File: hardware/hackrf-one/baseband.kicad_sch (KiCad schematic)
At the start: 98 parts, among them P14 XCVR_CLKOUT, P39 SSP1_SCK, P40 SSP1_COPI, P41 SSP1_CIPO, P53 CS_XCVR, P54 CS_AD, P56 RXENABLE, P61 DA0, P62 DA7, P63 DD0, P64 DD9, P65 DA4, P66 DD5, P67 RSSI, P83 GND, P84 GND, P85 GND, P86 GND, P87 GND, P88 GND, P89 GND, P9 BASEBAND, P90 GND, P91 GND, P92 GND, Q3 MOSFET_P, T3 RX_BALUN, T4 TX_BALUN, U17 MAX2839, U18 MAX5864

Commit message: HackRF One: update 100 nF capacitor part selection
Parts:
- C123, C167, C71, C73, C75, C77, C79, C81, C83, C91: Manufacturer Murata -> Samsung; Part Number GRM155R61A104KA01D -> CL05A104KA5NNNC
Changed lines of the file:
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@@
       (effects (font (size 1.524 1.524)) hide)
     )
-    (property "Manufacturer" "Murata" (id 4) (at 388.62 190.5 0)
-      (effects (font (size 1.524 1.524)) hide)
-    )
-    (property "Part Number" "GRM155R61A104KA01D" (id 5) (at 388.62 190.5 0)
-      (effects (font (size 1.524 1.524)) hide)
-    )
-    (property "Description" "CAP CER 0.1UF 10V 10% X5R 0402" (id 6) (at 388.62 190.5 0)
+    (property "Manufacturer" "Samsung" (id 4) (at 388.62 190.5 0)
+      (effects (font (size 1.524 1.524)) hide)
+    )
+    (property "Part Number" "CL05A104KA5NNNC" (id 5) (at 388.62 190.5 0)
+      (effects (font (size 1.524 1.524)) hide)
+    )
+    (property "Description" "CAP CER 0.1UF 25V X5R 0402" (id 6) (at 388.62 190.5 0)
       (effects (font (size 1.524 1.524)) hide)
     )
@@
       (effects (font (size 1.524 1.524)) hide)
     )
-    (property "Manufacturer" "Murata" (id 4) (at 303.53 30.48 0)
-      (effects (font (size 1.524 1.524)) hide)
-    )
-    (property "Part Number" "GRM155R61A104KA01D" (id 5) (at 303.53 30.48 0)
-      (effects (font (size 1.524 1.524)) hide)
-    )
-    (property "Description" "CAP CER 0.1UF 10V 10% X5R 0402" (id 6) (at 303.53 30.48 0)
+    (property "Manufacturer" "Samsung" (id 4) (at 303.53 30.48 0)
+      (effects (font (size 1.524 1.524)) hide)
+    )
+    (property "Part Number" "CL05A104KA5NNNC" (id 5) (at 303.53 30.48 0)
+      (effects (font (size 1.524 1.524)) hide)
+    )
+    (property "Description" "CAP CER 0.1UF 25V X5R 0402" (id 6) (at 303.53 30.48 0)
       (effects (font (size 1.524 1.524)) hide)
     )
@@
       (effects (font (size 1.524 1.524)) hide)
     )
-    (property "Manufacturer" "Murata" (id 4) (at 318.77 30.48 0)
-      (effects (font (size 1.524 1.524)) hide)
-    )
-    (property "Part Number" "GRM155R61A104KA01D" (id 5) (at 318.77 30.48 0)
-      (effects (font (size 1.524 1.524)) hide)
-    )
-    (property "Description" "CAP CER 0.1UF 10V 10% X5R 0402" (id 6) (at 318.77 30.48 0)
+    (property "Manufacturer" "Samsung" (id 4) (at 318.77 30.48 0)
+      (effects (font (size 1.524 1.524)) hide)
+    )
+    (property "Part Number" "CL05A104KA5NNNC" (id 5) (at 318.77 30.48 0)
+      (effects (font (size 1.524 1.524)) hide)
+    )
+    (property "Description" "CAP CER 0.1UF 25V X5R 0402" (id 6) (at 318.77 30.48 0)
       (effects (font (size 1.524 1.524)) hide)
     )
@@
       (effects (font (size 1.524 1.524)) hide)
     )
-    (property "Manufacturer" "Murata" (id 4) (at 334.01 30.48 0)
-      (effects (font (size 1.524 1.524)) hide)
-    )
-    (property "Part Number" "GRM155R61A104KA01D" (id 5) (at 334.01 30.48 0)
-      (effects (font (size 1.524 1.524)) hide)
-    )
-    (property "Description" "CAP CER 0.1UF 10V 10% X5R 0402" (id 6) (at 334.01 30.48 0)
+    (property "Manufacturer" "Samsung" (id 4) (at 334.01 30.48 0)
+      (effects (font (size 1.524 1.524)) hide)
+    )
+    (property "Part Number" "CL05A104KA5NNNC" (id 5) (at 334.01 30.48 0)
+      (effects (font (size 1.524 1.524)) hide)
+    )
+    (property "Description" "CAP CER 0.1UF 25V X5R 0402" (id 6) (at 334.01 30.48 0)
       (effects (font (size 1.524 1.524)) hide)
     )
@@
       (effects (font (size 1.524 1.524)) hide)
     )
-    (property "Manufacturer" "Murata" (id 4) (at 349.25 30.48 0)
-      (effects (font (size 1.524 1.524)) hide)
-    )
-    (property "Part Number" "GRM155R61A104KA01D" (id 5) (at 349.25 30.48 0)
-      (effects (font (size 1.524 1.524)) hide)
-    )
-    (property "Description" "CAP CER 0.1UF 10V 10% X5R 0402" (id 6) (at 349.25 30.48 0)
+    (property "Manufacturer" "Samsung" (id 4) (at 349.25 30.48 0)
+      (effects (font (size 1.524 1.524)) hide)
+    )
+    (property "Part Number" "CL05A104KA5NNNC" (id 5) (at 349.25 30.48 0)
+      (effects (font (size 1.524 1.524)) hide)
+    )
+    (property "Description" "CAP CER 0.1UF 25V X5R 0402" (id 6) (at 349.25 30.48 0)
       (effects (font (size 1.524 1.524)) hide)
     )
@@
       (effects (font (size 1.524 1.524)) hide)
     )
-    (property "Manufacturer" "Murata" (id 4) (at 364.49 30.48 0)
-      (effects (font (size 1.524 1.524)) hide)
-    )
-    (property "Part Number" "GRM155R61A104KA01D" (id 5) (at 364.49 30.48 0)
-      (effects (font (size 1.524 1.524)) hide)
-    )
-    (property "Description" "CAP CER 0.1UF 10V 10% X5R 0402" (id 6) (at 364.49 30.48 0)
+    (property "Manufacturer" "Samsung" (id 4) (at 364.49 30.48 0)
+      (effects (font (size 1.524 1.524)) hide)
+    )
+    (property "Part Number" "CL05A104KA5NNNC" (id 5) (at 364.49 30.48 0)
+      (effects (font (size 1.524 1.524)) hide)
+    )
+    (property "Description" "CAP CER 0.1UF 25V X5R 0402" (id 6) (at 364.49 30.48 0)
       (effects (font (size 1.524 1.524)) hide)
     )
@@
       (effects (font (size 1.524 1.524)) hide)
     )
-    (property "Manufacturer" "Murata" (id 4) (at 379.73 30.48 0)
-      (effects (font (size 1.524 1.524)) hide)
-    )
-    (property "Part Number" "GRM155R61A104KA01D" (id 5) (at 379.73 30.48 0)
-      (effects (font (size 1.524 1.524)) hide)
-    )
-    (property "Description" "CAP CER 0.1UF 10V 10% X5R 0402" (id 6) (at 379.73 30.48 0)
+    (property "Manufacturer" "Samsung" (id 4) (at 379.73 30.48 0)
+      (effects (font (size 1.524 1.524)) hide)
+    )
+    (property "Part Number" "CL05A104KA5NNNC" (id 5) (at 379.73 30.48 0)
+      (effects (font (size 1.524 1.524)) hide)
+    )
+    (property "Description" "CAP CER 0.1UF 25V X5R 0402" (id 6) (at 379.73 30.48 0)
       (effects (font (size 1.524 1.524)) hide)
     )
@@
       (effects (font (size 1.524 1.524)) hide)
     )
-    (property "Manufacturer" "Murata" (id 4) (at 394.97 30.48 0)
-      (effects (font (size 1.524 1.524)) hide)
-    )
-    (property "Part Number" "GRM155R61A104KA01D" (id 5) (at 394.97 30.48 0)
-      (effects (font (size 1.524 1.524)) hide)
-    )
-    (property "Description" "CAP CER 0.1UF 10V 10% X5R 0402" (id 6) (at 394.97 30.48 0)
+    (property "Manufacturer" "Samsung" (id 4) (at 394.97 30.48 0)
+      (effects (font (size 1.524 1.524)) hide)
+    )
+    (property "Part Number" "CL05A104KA5NNNC" (id 5) (at 394.97 30.48 0)
+      (effects (font (size 1.524 1.524)) hide)
+    )
+    (property "Description" "CAP CER 0.1UF 25V X5R 0402" (id 6) (at 394.97 30.48 0)
       (effects (font (size 1.524 1.524)) hide)
     )
@@
       (effects (font (size 1.524 1.524)) hide)
     )
-    (property "Manufacturer" "Murata" (id 4) (at 87.63 31.75 0)
-      (effects (font (size 1.524 1.524)) hide)
-    )
-    (property "Part Number" "GRM155R61A104KA01D" (id 5) (at 87.63 31.75 0)
-      (effects (font (size 1.524 1.524)) hide)
-    )
-    (property "Description" "CAP CER 0.1UF 10V 10% X5R 0402" (id 6) (at 87.63 31.75 0)
+    (property "Manufacturer" "Samsung" (id 4) (at 87.63 31.75 0)
+      (effects (font (size 1.524 1.524)) hide)
+    )
+    (property "Part Number" "CL05A104KA5NNNC" (id 5) (at 87.63 31.75 0)
+      (effects (font (size 1.524 1.524)) hide)
+    )
+    (property "Description" "CAP CER 0.1UF 25V X5R 0402" (id 6) (at 87.63 31.75 0)
       (effects (font (size 1.524 1.524)) hide)
     )
@@
       (effects (font (size 1.524 1.524)) hide)
     )
-    (property "Manufacturer" "Murata" (id 4) (at 40.64 64.77 0)
-      (effects (font (size 1.524 1.524)) hide)
-    )
-    (property "Part Number" "GRM155R61A104KA01D" (id 5) (at 40.64 64.77 0)
-      (effects (font (size 1.524 1.524)) hide)
-    )
-    (property "Description" "CAP CER 0.1UF 10V 10% X5R 0402" (id 6) (at 40.64 64.77 0)
-      (effects (font (size 1.524 1.524)) hide)
-    )
+    (property "Manufacturer" "Samsung" (id 4) (at 40.64 64.77 0)
+      (effects (font (size 1.524 1.524)) hide)
+    )
+    (property "Part Number" "CL05A104KA5NNNC" (id 5) (at 40.64 64.77 0)
+      (effects (font (size 1.524 1.524)) hide)
+    )
+    (property "Description" "CAP CER 0.1UF 25V X5R 0402" (id 6) (at 40.64 64.77 0)
+      (effects (font (size 1.524 1.524)) hide)
+    )

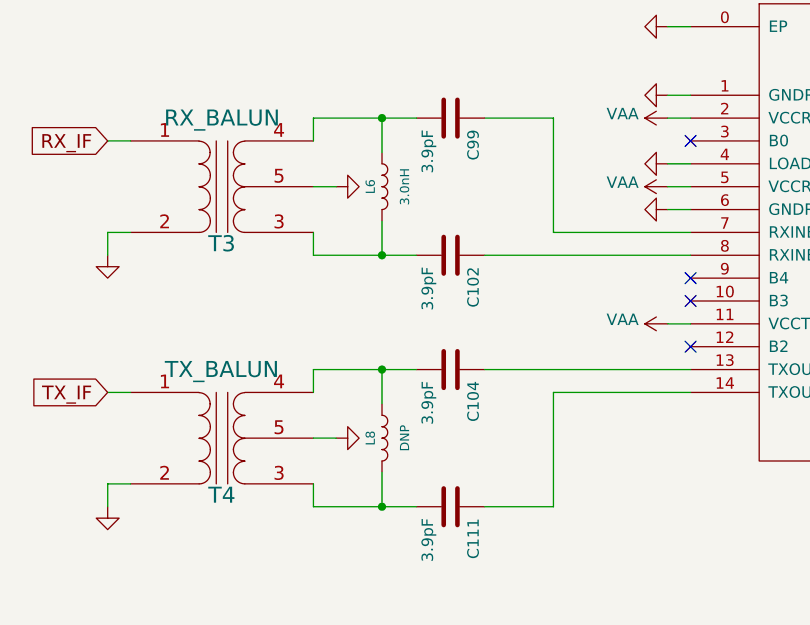
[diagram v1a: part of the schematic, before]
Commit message: HackRF One: update IF balun tuning inductors
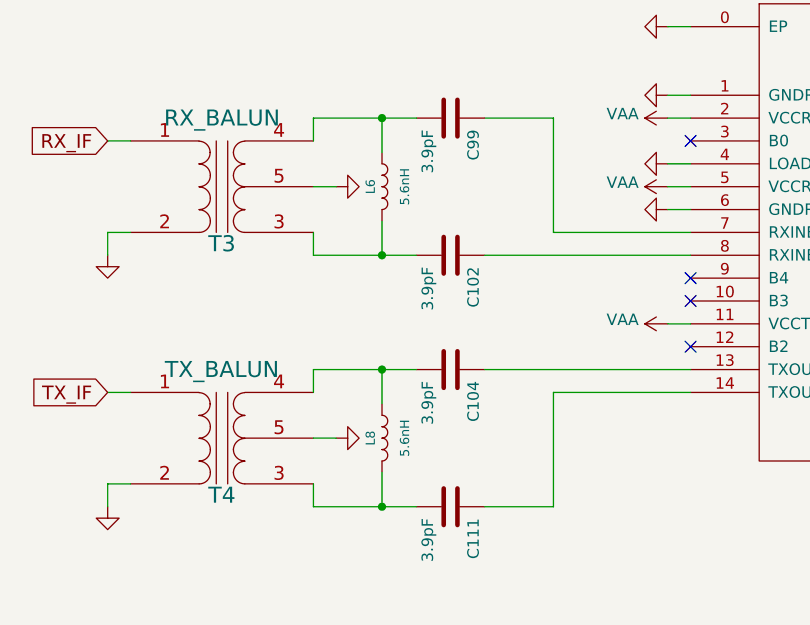
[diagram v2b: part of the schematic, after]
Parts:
- L6: value 3.0nH -> 5.6nH; Part Number LQG15HS3N0B02D -> LQG15HS5N6S02D
- L8: value DNP -> 5.6nH; DNP DNP -> (none); Manufacturer (none) -> Murata; Part Number (none) -> LQG15HS5N6S02D
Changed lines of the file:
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@@
       (effects (font (size 1.016 1.016)))
     )
-    (property "Value" "3.0nH" (id 1) (at 130.81 120.65 90)
+    (property "Value" "5.6nH" (id 1) (at 130.81 120.65 90)
       (effects (font (size 1.016 1.016)))
     )
@@
       (effects (font (size 1.524 1.524)) hide)
     )
-    (property "Description" "FIXED IND 3NH 800MA 125MOHM ±0.1nH SMD" (id 4) (at 128.27 120.65 0)
+    (property "Description" "FIXED IND 5.6NH 650MA 200MOHM ±0.3nH SMD" (id 4) (at 128.27 120.65 0)
       (effects (font (size 1.27 1.27)) hide)
     )
@@
       (effects (font (size 1.27 1.27)) hide)
     )
-    (property "Part Number" "LQG15HS3N0B02D" (id 6) (at 128.27 120.65 0)
+    (property "Part Number" "LQG15HS5N6S02D" (id 6) (at 128.27 120.65 0)
       (effects (font (size 1.27 1.27)) hide)
     )
@@
       (effects (font (size 1.016 1.016)))
     )
-    (property "Value" "DNP" (id 1) (at 130.81 148.59 90)
+    (property "Value" "5.6nH" (id 1) (at 130.81 148.59 90)
       (effects (font (size 1.016 1.016)))
     )
@@
       (effects (font (size 1.524 1.524)) hide)
     )
-    (property "DNP" "DNP" (id 4) (at 128.27 148.59 0)
+    (property "DNP" "" (id 4) (at 128.27 148.59 0)
       (effects (font (size 1.524 1.524)) hide)
     )
+    (property "Description" "FIXED IND 5.6NH 650MA 200MOHM ±0.3nH SMD" (id 5) (at 128.27 148.59 0)
+      (effects (font (size 1.27 1.27)) hide)
+    )
+    (property "Manufacturer" "Murata" (id 6) (at 128.27 148.59 0)
+      (effects (font (size 1.27 1.27)) hide)
+    )
+    (property "Part Number" "LQG15HS5N6S02D" (id 7) (at 128.27 148.59 0)
+      (effects (font (size 1.27 1.27)) hide)
+    )
     (pin "1")

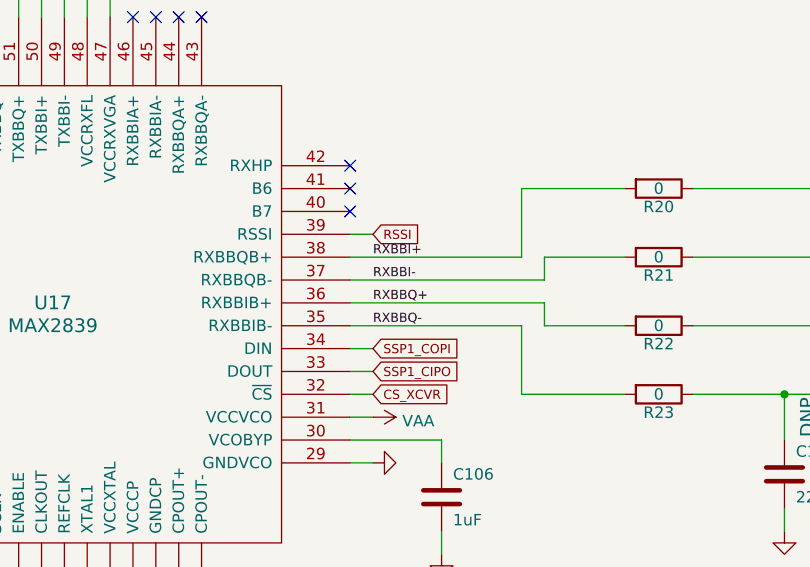
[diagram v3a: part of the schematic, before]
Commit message: HackRF One: correct RXBB net names
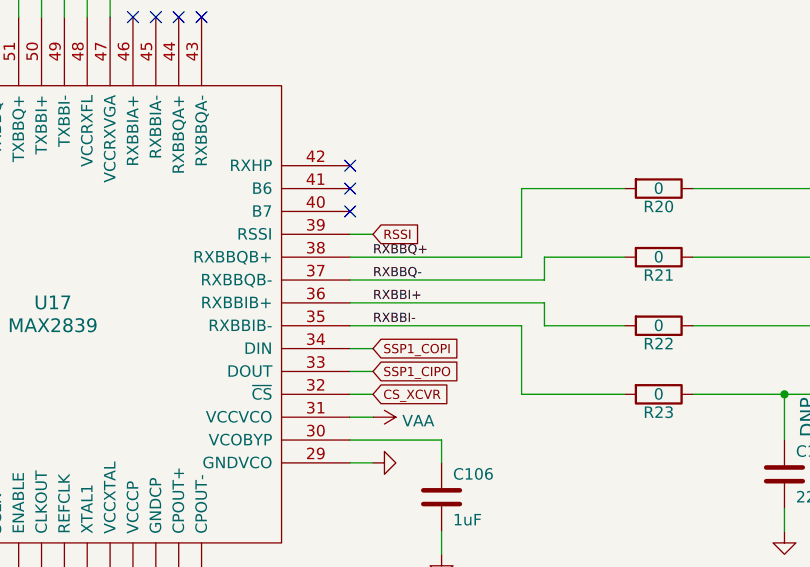
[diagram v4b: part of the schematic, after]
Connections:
- net RXBBI+: now also R22.2, U17.36 (RXBBIB+); no longer R20.2, U17.38 (RXBBQB+)
- net RXBBI-: now also R23.2, U17.35 (RXBBIB-); no longer R21.2, U17.37 (RXBBQB-)
- net RXBBQ+: now also R20.2, U17.38 (RXBBQB+); no longer R22.2, U17.36 (RXBBIB+)
- net RXBBQ-: now also R21.2, U17.37 (RXBBQB-); no longer R23.2, U17.35 (RXBBIB-)
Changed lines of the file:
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@@
     (effects (font (size 1.016 1.016)) (justify left bottom))
   )
-  (label "RXBBQ-" (at 231.14 127 0)
+  (label "RXBBI-" (at 231.14 127 0)
     (effects (font (size 1.016 1.016)) (justify left bottom))
   )
@@
     (effects (font (size 1.016 1.016)) (justify left bottom))
   )
-  (label "RXBBQ+" (at 231.14 124.46 0)
+  (label "RXBBI+" (at 231.14 124.46 0)
     (effects (font (size 1.016 1.016)) (justify left bottom))
   )
@@
     (effects (font (size 1.016 1.016)) (justify left bottom))
   )
-  (label "RXBBI+" (at 231.14 119.38 0)
+  (label "RXBBQ+" (at 231.14 119.38 0)
     (effects (font (size 1.016 1.016)) (justify left bottom))
   )
@@
     (effects (font (size 1.016 1.016)) (justify left bottom))
   )
-  (label "RXBBI-" (at 231.14 121.92 0)
+  (label "RXBBQ-" (at 231.14 121.92 0)
     (effects (font (size 1.016 1.016)) (justify left bottom))
   )
